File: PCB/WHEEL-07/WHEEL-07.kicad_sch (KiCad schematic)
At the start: 0 parts

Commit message: PCB schematics with MCU
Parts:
- added C1, C2: 2u2, symbol Device:C_Small
- added C3, C4, C5, C6: 10pF, Capacitor_SMD:C_0402_1005Metric_Pad0.74x0.62mm_HandSolder, symbol Device:C_Small
- added C7, C8: 100n, Capacitor_SMD:C_0402_1005Metric_Pad0.74x0.62mm_HandSolder, symbol Device:C_Small
- added C9: 1u, Capacitor_SMD:C_0402_1005Metric_Pad0.74x0.62mm_HandSolder, symbol Device:C_Small
- added D?: LED_Small, symbol Device:LED_Small
- added JP1: SolderJumper_3_Open, symbol Jumper:SolderJumper_3_Open
- added L1: 2u7 120m, symbol Device:L_Small
- added R1: 1k, Resistor_SMD:R_0402_1005Metric_Pad0.72x0.64mm_HandSolder, symbol Device:R_Small
- added R? (x2): 2k2, symbol Device:R_Small
- added R?: 1k5, symbol Device:R_Small
- added U1: STM32F405RGTx, Package_QFP:LQFP-64_10x10mm_P0.5mm, symbol MCU_ST_STM32F4:STM32F405RGTx
- added Y1: 16Mhz, Crystal:Crystal_SMD_5032-2Pin_5.0x3.2mm, symbol Device:Crystal_Small
- added Y2: 32KHz, Crystal:Crystal_SMD_3215-2Pin_3.2x1.5mm, symbol Device:Crystal_Small
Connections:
- new net: D?.2 (A), R?.2
- new net: C2.1, U1.47 (VCAP_2)
- new net: JP1.2 (C), R1.2
- new net: C1.1, U1.31 (VCAP_1)
- new net +3.3V: C7.1, JP1.3 (B), L1.1, R?.1, R?.1, U1.1 (VBAT), U1.19 (VDD), U1.32 (VDD), U1.48 (VDD), U1.64 (VDD)
- new net +3.3VA: U1.13 (VDDA)
- new net ADC_A1: U1.8 (PC0)
- new net ADC_A2: U1.9 (PC1)
- new net ADC_A3: U1.10 (PC2)
- new net ADC_A4: U1.11 (PC3)
- new net ADC_B1: U1.14 (PA0)
- new net ADC_B2: U1.15 (PA1)
- new net ADC_B3: U1.16 (PA2)
- new net ADC_B4: U1.17 (PA3)
- new net BOOT0: R1.1, U1.60 (BOOT0)
- new net CAN1_RX: U1.61 (PB8)
- new net CAN1_TX: U1.62 (PB9)
- new net CAN2_RX: U1.57 (PB5)
- new net CAN2_TX: U1.58 (PB6)
- new net GND: C1.2, C2.2, C3.2, C4.2, C5.2, C6.2, C7.2, C8.2, C9.2, D?.1 (K), JP1.1 (A), U1.12 (VSSA), U1.18 (VSS)
- new net I2C2_SCL: R?.2, U1.29 (PB10)
- new net I2C2_SDA: R?.2, U1.30 (PB11)
- new net LED_STATUS: R?.1, U1.2 (PC13)
- new net NRST: U1.7 (NRST)
- new net OSC32_IN: C5.1, U1.3 (PC14), Y2.1
- new net OSC32_OUT: C6.1, U1.4 (PC15), Y2.2
- new net OSC_IN: C3.1, U1.5 (PH0), Y1.1
- new net OSC_OUT: C4.1, U1.6 (PH1), Y1.2
- new net SPI2_MISO: U1.35 (PB14)
- new net SPI2_MOSI: U1.36 (PB15)
- new net SPI2_SCK: U1.34 (PB13)
- new net SWCLK: U1.49 (PA14)
- new net SWDIO: U1.46 (PA13)
- new net SWO: U1.55 (PB3)
- new net TIM1_CH1: U1.41 (PA8)
- new net TIM1_CH2: U1.42 (PA9)
- new net TIM1_CH3: U1.43 (PA10)
- new net USART_CK: U1.53 (PC12)
- new net USART_RX: U1.52 (PC11)
- new net USART_TX: U1.51 (PC10)
- new net VDDA: C8.1, C9.1, L1.2
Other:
- note added: "BOOT"
- note added: "HSE"
- note added: "LSE"
- note added: "Use high-quality ceramic capacitors designed for high-frequency (5-20pF)."

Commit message: Finished schematics
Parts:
- added J1: Conn_01x06_Male, symbol Connector:Conn_01x06_Male
- R2, R3, R5: renamed from R?; footprint (none) -> Resistor_SMD:R_0402_1005Metric_Pad0.72x0.64mm_HandSolder
- gave numbers to parts that had none: 1
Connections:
- net GND: now also J1.6 (Pin_6)
- net GPIO_1: now reaches U1.20 (PA4)
- net GPIO_2: now reaches U1.21 (PA5)
- net GPIO_3: now reaches U1.22 (PA6)
- net GPIO_4: now reaches U1.23 (PA7)
- net GPIO_5: now reaches U1.24 (PC4)
- net GPIO_6: now reaches U1.25 (PC5)
- net GPIO_7: now reaches U1.26 (PB0)
- net GPIO_8: now reaches U1.27 (PB1)
- net SPI_CS: now reaches U1.33 (PB12)
- new net +12V: J1.5 (Pin_5)
- new net CAN_BUS/CAN1_H: J1.2 (Pin_2)
- new net CAN_BUS/CAN1_L: J1.1 (Pin_1)
- new net CAN_BUS/CAN2_H: J1.4 (Pin_4)
- new net CAN_BUS/CAN2_L: J1.3 (Pin_3)
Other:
- added sheet CAN_BUS (can_bus.kicad_sch)
- added sheet HEADERS (headers.kicad_sch)
- added sheet POWER (power.kicad_sch)
- note added: "VDDA filter"
- moved on the sheet: C7, C8, C9, D1, JP1, L1, R1, R5

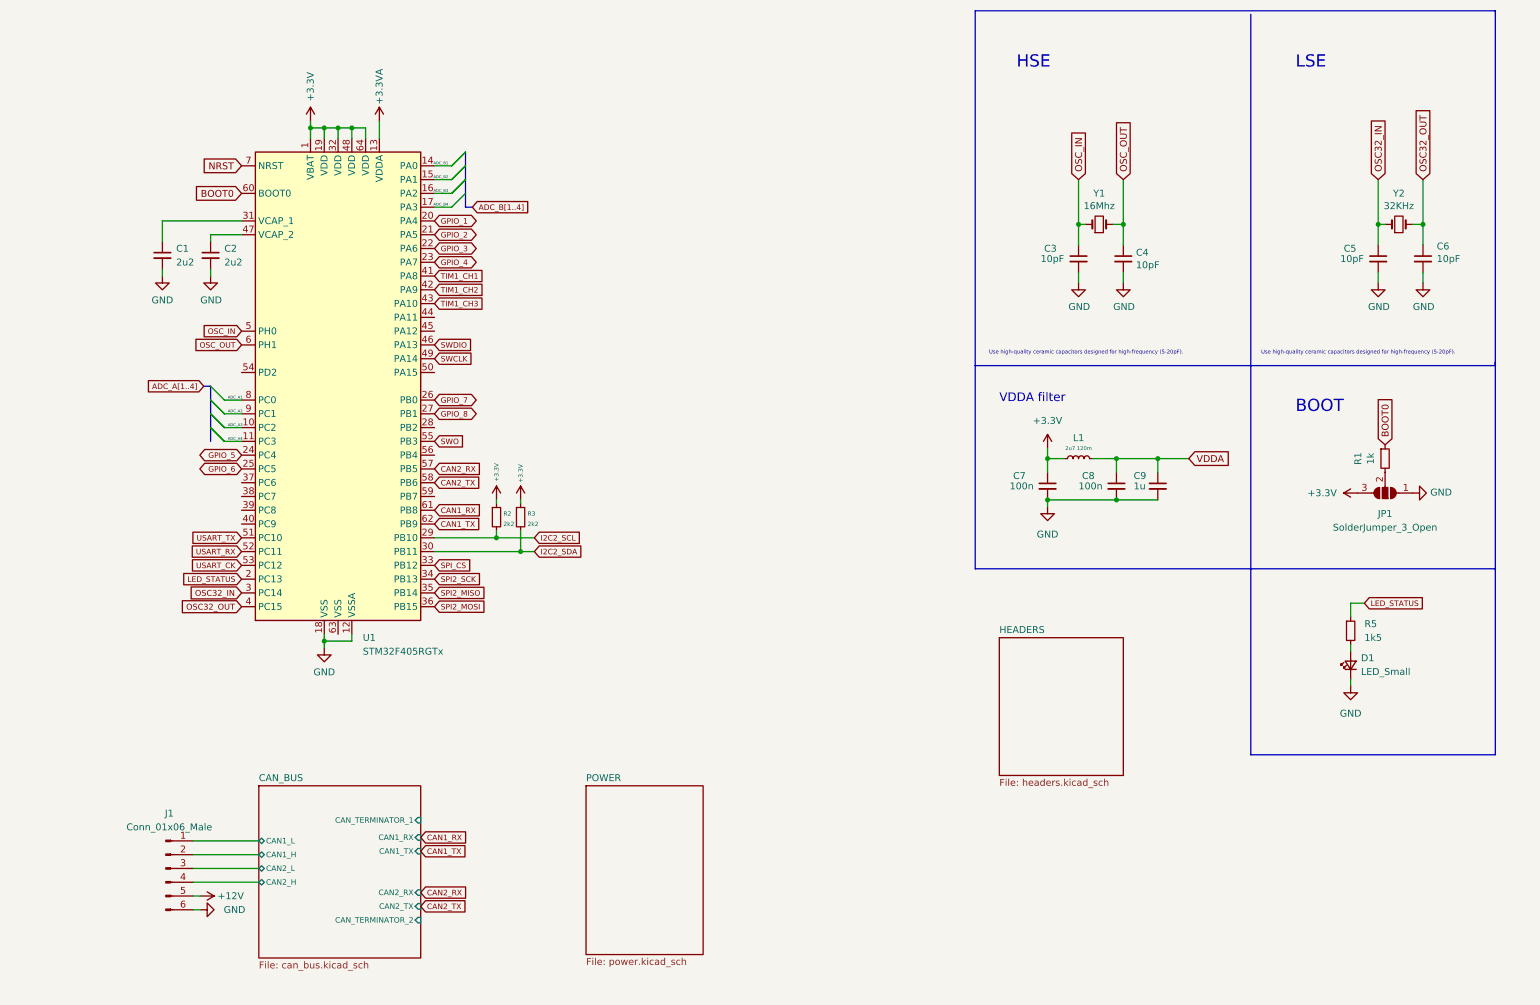
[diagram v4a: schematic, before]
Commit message: Modified layout
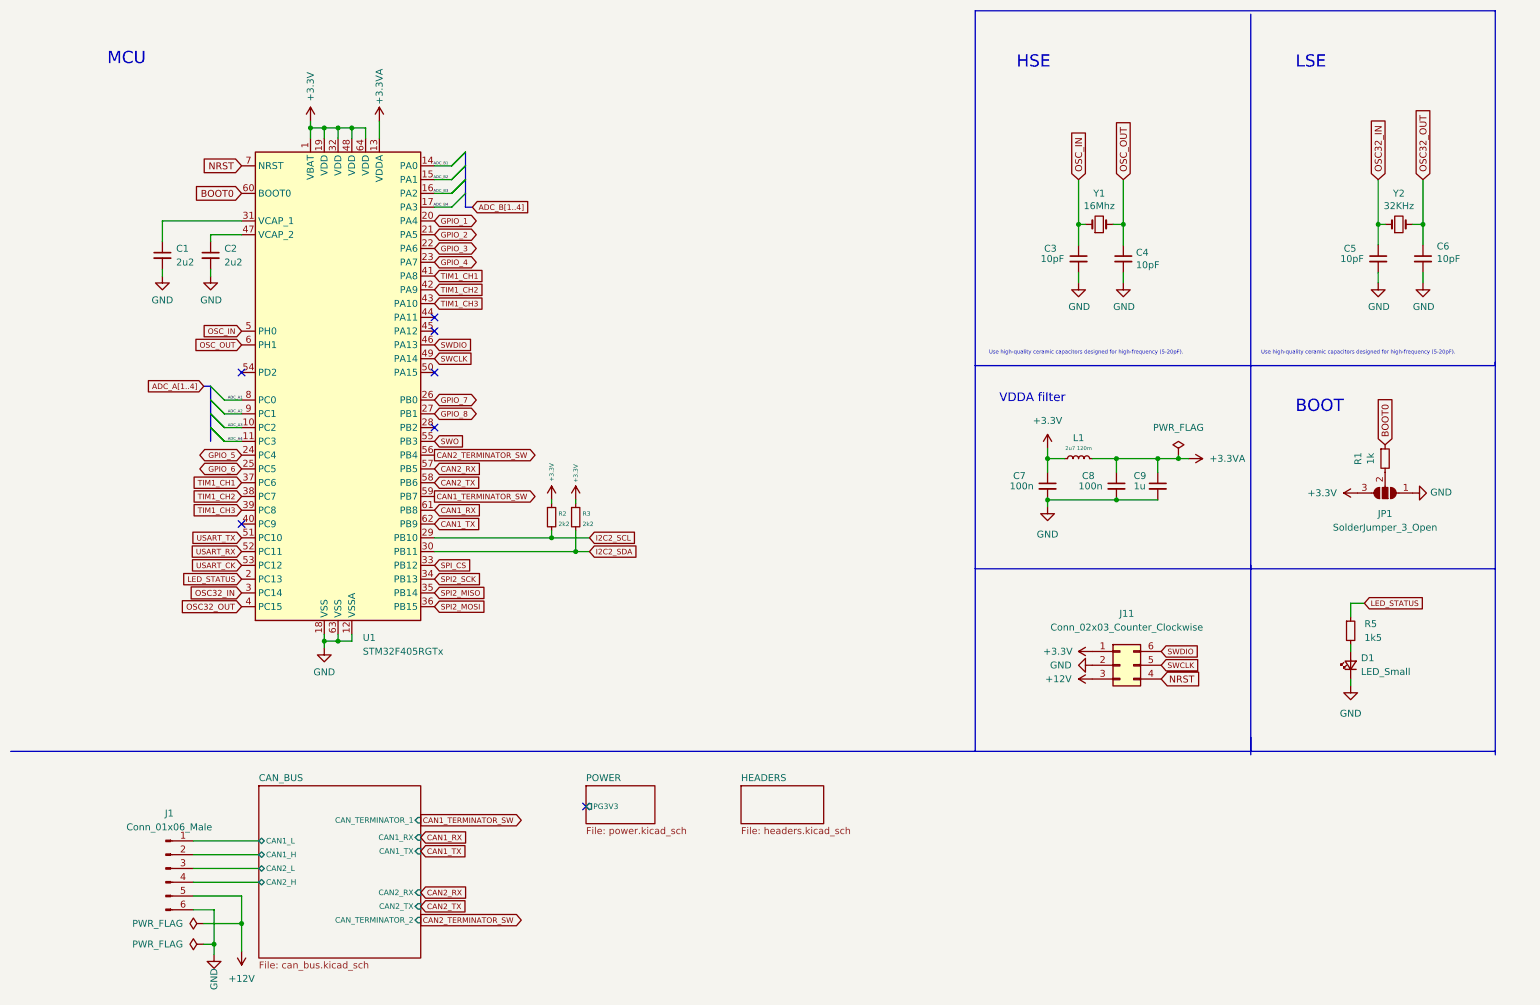
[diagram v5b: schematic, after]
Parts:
- added J11: Conn_02x03_Counter_Clockwise, Connector_PinHeader_2.54mm:PinHeader_2x03_P2.54mm_Vertical, symbol Connector_Generic:Conn_02x03_Counter_Clockwise
- JP1: footprint (none) -> Jumper:SolderJumper-3_P1.3mm_Open_RoundedPad1.0x1.5mm
- R1, R2, R3, R5: footprint Resistor_SMD:R_0402_1005Metric_Pad0.72x0.64mm_HandSolder -> Resistor_SMD:R_0402_1005Metric
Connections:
- net VDDA is gone; now on net +3.3VA: C8.1, C9.1, L1.2
- net +12V: now also J11.3 (Pin_3)
- net +3.3V: now also J11.1 (Pin_1)
- net GND: now also U1.63 (VSS), J11.2 (Pin_2)
- net NRST: now also J11.4 (Pin_4)
- net SWCLK: now also J11.5 (Pin_5)
- net SWDIO: now also J11.6 (Pin_6)
- net TIM1_CH1: now also U1.37 (PC6)
- net TIM1_CH2: now also U1.38 (PC7)
- net TIM1_CH3: now also U1.39 (PC8)
- net CAN2_TERMINATOR_SW: now reaches U1.56 (PB4)
- net CAN1_TERMINATOR_SW: now reaches U1.59 (PB7)
- no-connect marks 0 -> 7
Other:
- sheet POWER ports: added PG3V3; removed none
- note added: "MCU"
- moved on the sheet: R2, R3

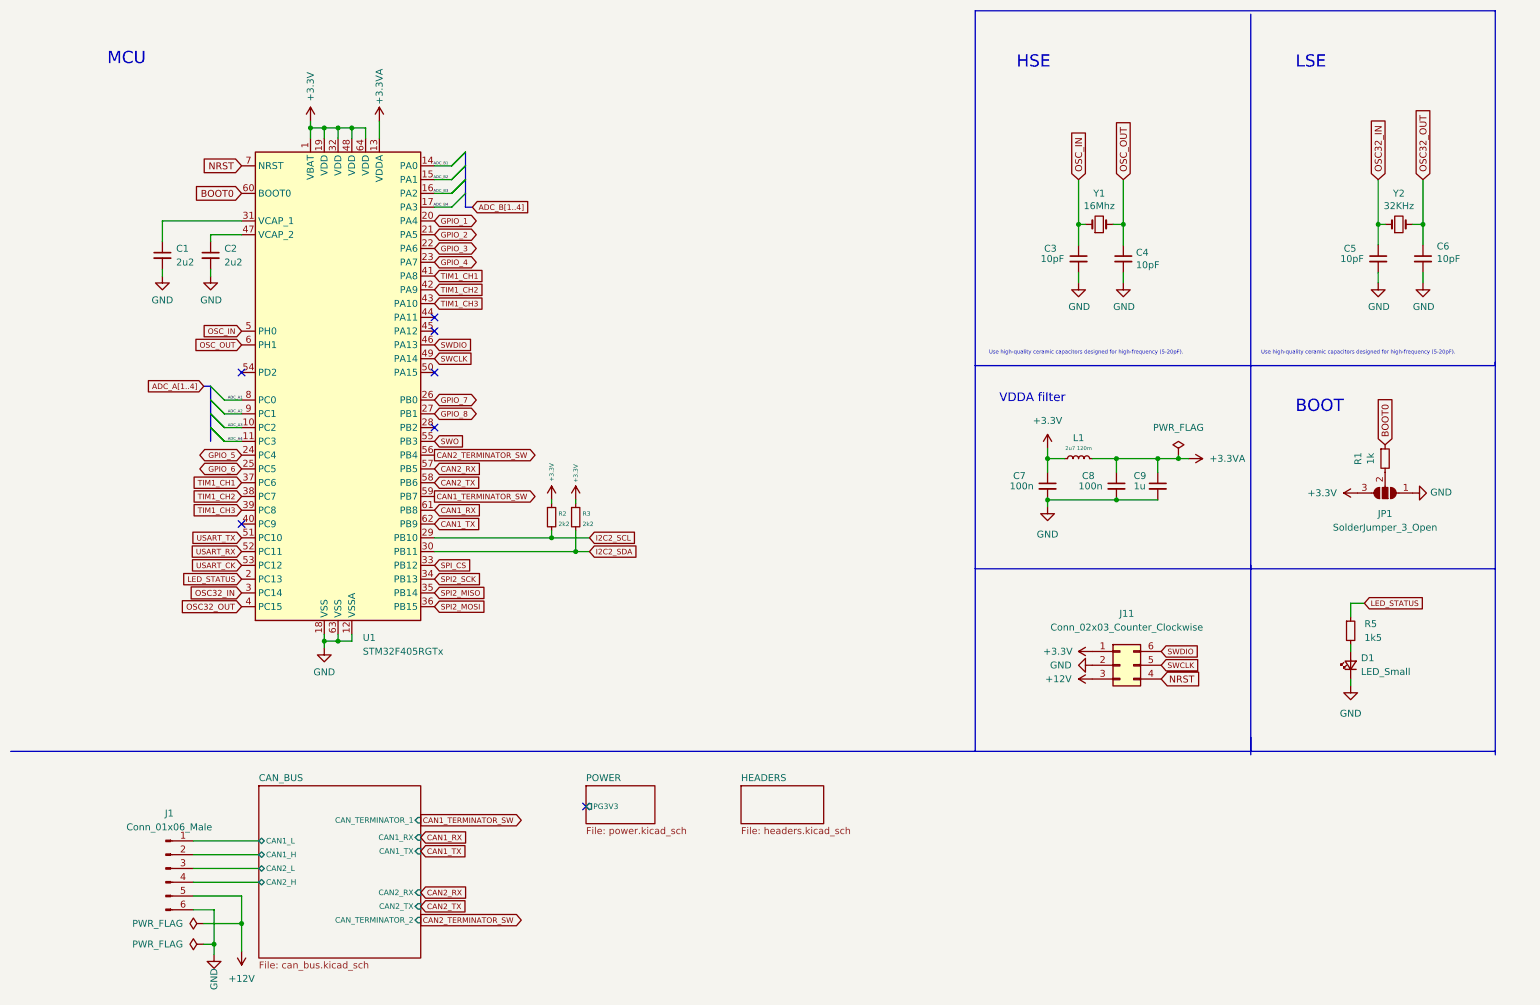
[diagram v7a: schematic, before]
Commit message: Modified schematics & assigned all footprints
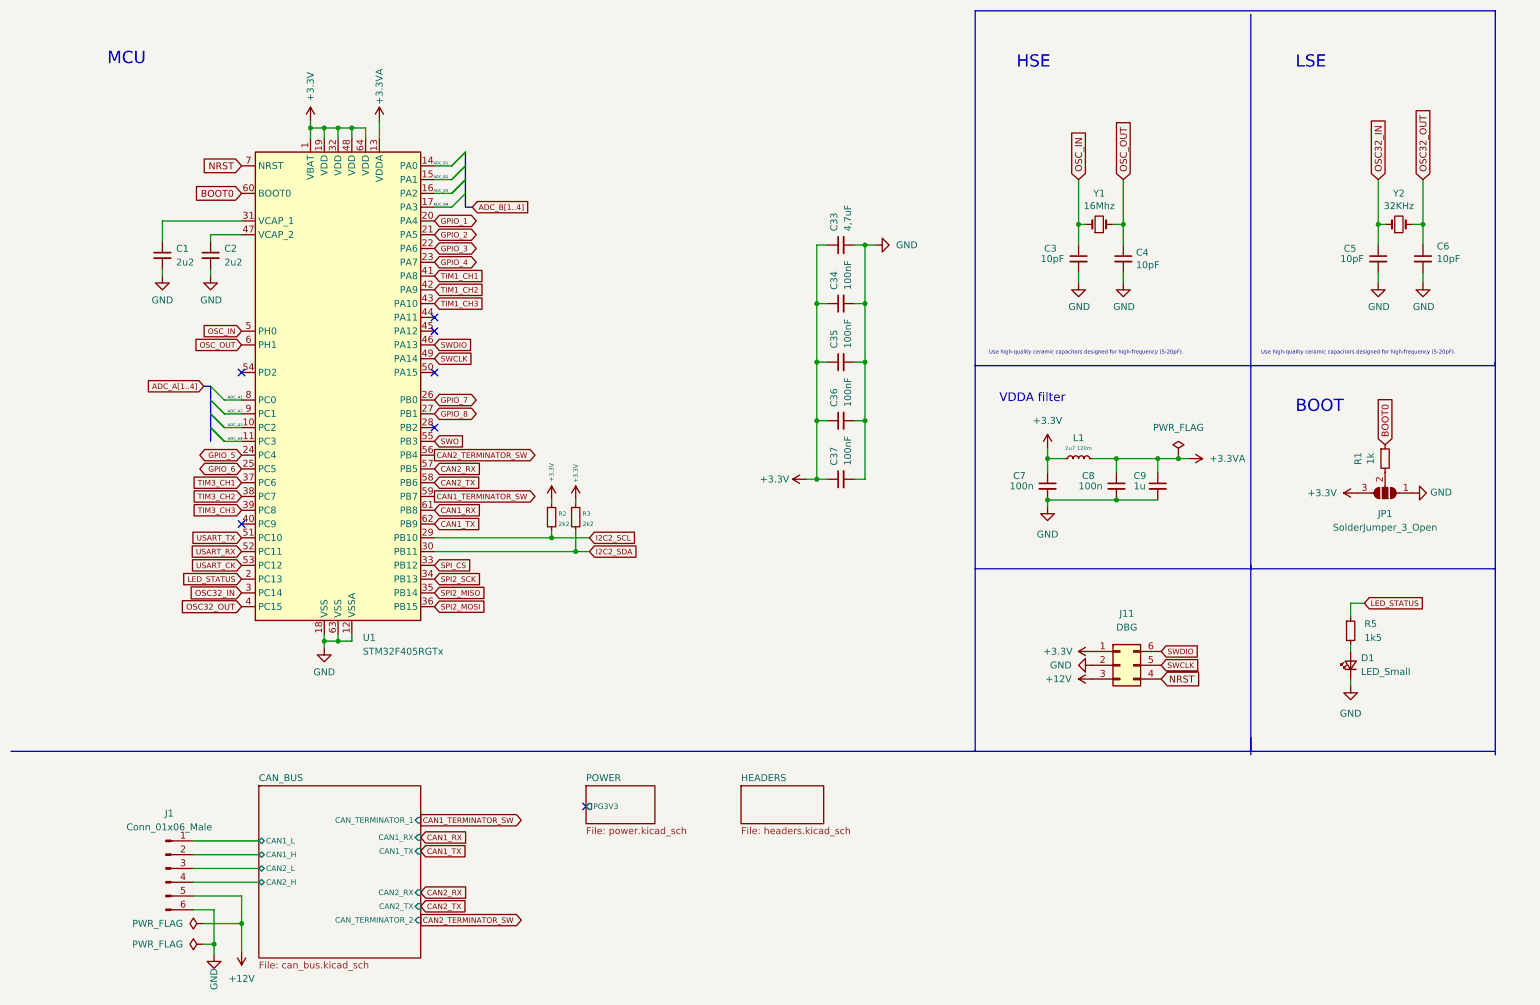
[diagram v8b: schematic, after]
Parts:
- added C33: 4,7uF, Capacitor_SMD:C_0201_0603Metric, symbol Device:C_Small
- added C34, C35, C36, C37: 100nF, Capacitor_SMD:C_0402_1005Metric, symbol Device:C_Small
- C1, C2: footprint (none) -> Capacitor_SMD:C_0402_1005Metric
- C3, C4, C5, C6, C7, C8: footprint Capacitor_SMD:C_0402_1005Metric_Pad0.74x0.62mm_HandSolder -> Capacitor_SMD:C_0402_1005Metric
- D1: footprint (none) -> LED_SMD:LED_0805_2012Metric
- J11: value Conn_02x03_Counter_Clockwise -> DBG; footprint Connector_PinHeader_2.54mm:PinHeader_2x03_P2.54mm_Vertical -> Connector_PinHeader_1.27mm:PinHeader_2x03_P1.27mm_Vertical
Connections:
- net +3.3V: now also C33.1, C34.1, C35.1, C36.1, C37.1
- net GND: now also C33.2, C34.2, C35.2, C36.2, C37.2
- net TIM1_CH1: no longer U1.37 (PC6)
- net TIM1_CH2: no longer U1.38 (PC7)
- net TIM1_CH3: no longer U1.39 (PC8)
- new net TIM3_CH1: U1.37 (PC6)
- new net TIM3_CH2: U1.38 (PC7)
- new net TIM3_CH3: U1.39 (PC8)
